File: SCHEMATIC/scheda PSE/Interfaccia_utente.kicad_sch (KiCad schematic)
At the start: 18 parts

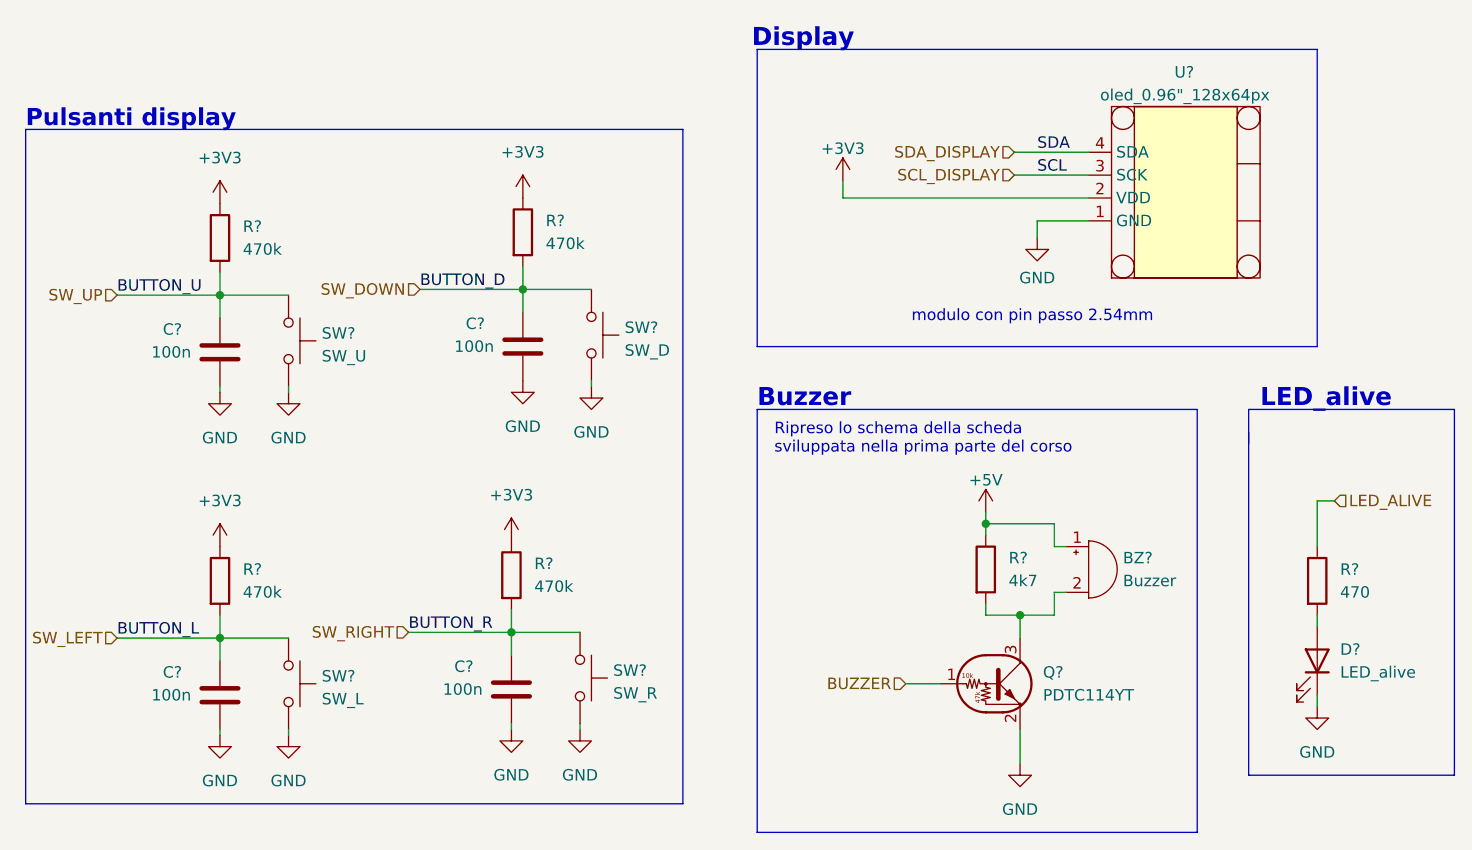
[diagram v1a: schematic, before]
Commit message: Aggiunti QUASI tutti i footprint
aggiunti quasi tutti i footprint dei componenti
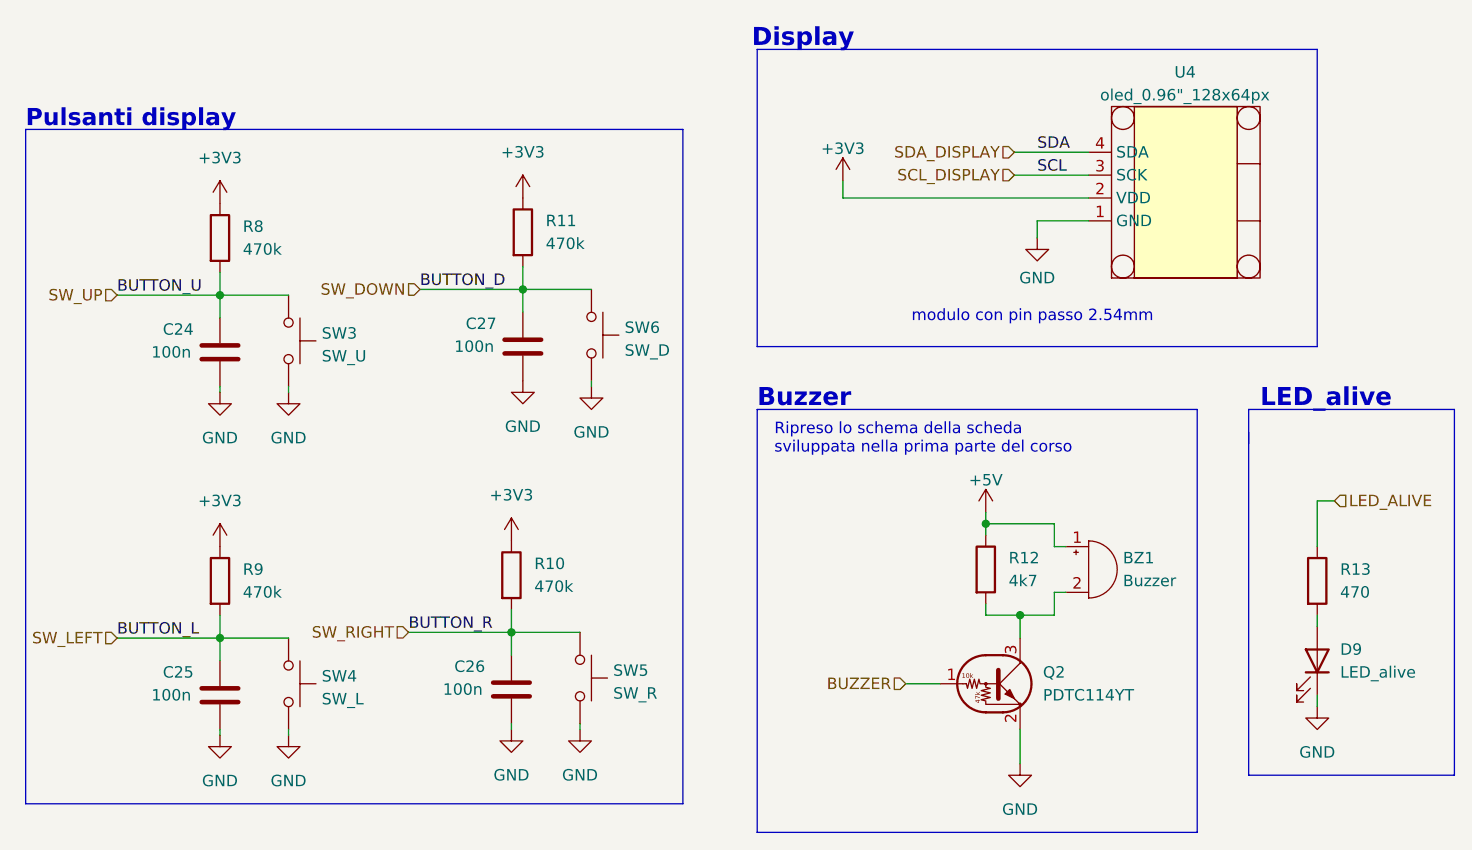
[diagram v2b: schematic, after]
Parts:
- C24, C25, C26, C27: renamed from C?; footprint (none) -> Capacitor_SMD:C_0603_1608Metric
- D9: renamed from D?; footprint (none) -> LED_SMD:LED_0603_1608Metric
- R10, R11, R13, R8, R9: renamed from R?; footprint (none) -> Resistor_SMD:R_0603_1608Metric
- SW3, SW4, SW5, SW6: renamed from SW?; footprint (none) -> Button_Switch_THT:SW_PUSH_6mm_H5mm
- U4: renamed from U?; footprint (none) -> _PSE:128x64OLED
- gave numbers to parts that had none: 3

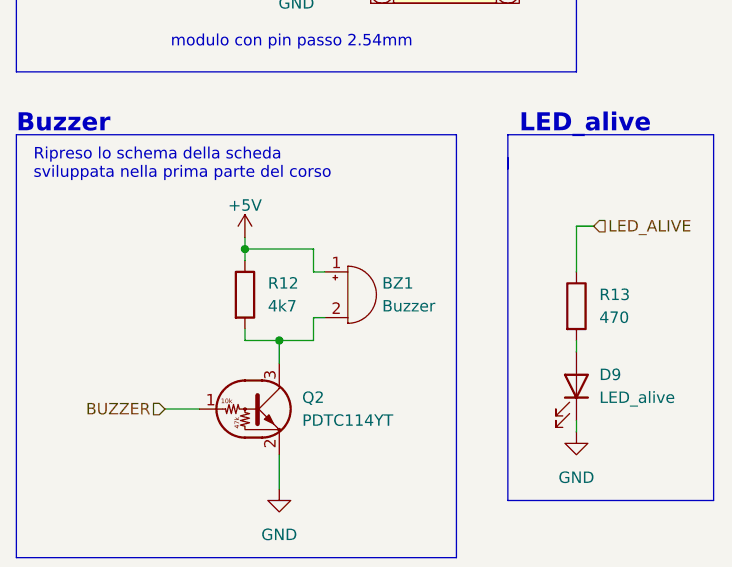
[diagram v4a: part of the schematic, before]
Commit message: sistemato buzzer, e continuato lo sbroglio
sistemato il buzzer con un altro footprint e ho continuato lo sbroglio.
Teoricamente manca solo collegare i collegamenti tra le gpio del rp2040 e il resto dei componenti
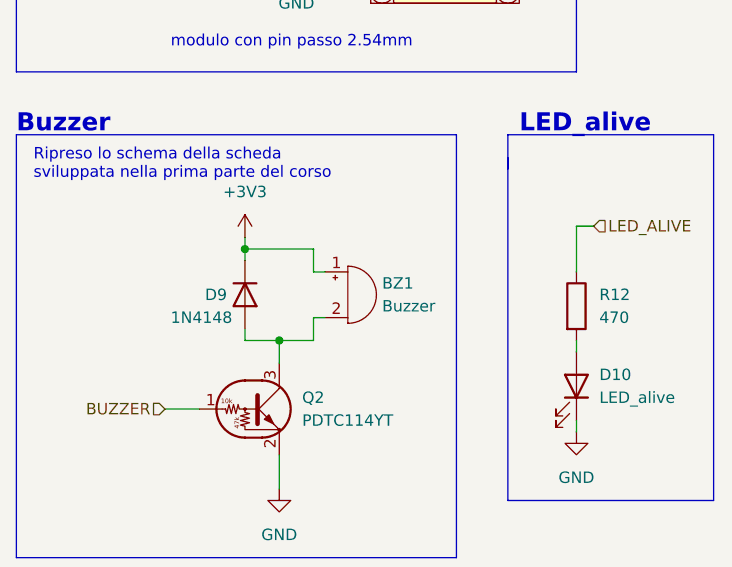
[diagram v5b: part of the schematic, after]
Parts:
- removed R12: 4k7, Resistor_SMD:R_0603_1608Metric, symbol Device:R
- added D9: 1N4148, Diode_SMD:D_SOD-123, symbol Diode:1N4148
- BZ1: footprint Buzzer_Beeper:MagneticBuzzer_Kingstate_KCG0601 -> _PSE:MLT-8530
- renumbered D9 to D10, R13 to R12
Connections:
- net +5V is gone; now on net +3V3: BZ1.1 (-)
- net +3V3: now also D9.1 (K)
- net at BZ1.2 (+), Q2.3 (C): now also D9.2 (A)
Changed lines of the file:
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@@
+    (pin "1")
+  )
+  (symbol (lib_id "power:+3V3") (at 187.96 98.425 0) (unit 1)
+    (in_bom yes) (on_board yes) (fields_autoplaced)
+    (property "Reference" "#PWR040" (id 0) (at 187.96 102.235 0)
+      (effects (font (size 1.27 1.27)) hide)
+    )
+    (property "Value" "+3V3" (id 1) (at 187.96 93.345 0))
+    (property "Footprint" "" (id 2) (at 187.96 98.425 0)
+      (effects (font (size 1.27 1.27)) hide)
+    )
+    (property "Datasheet" "" (id 3) (at 187.96 98.425 0)
+      (effects (font (size 1.27 1.27)) hide)
+    )
     (pin "1")
   )
@@
   (symbol (lib_id "Device:LED") (at 224.79 114.935 270) (mirror x) (unit 1)
     (in_bom yes) (on_board yes)
-    (property "Reference" "D9" (id 0) (at 227.33 113.665 90)
+    (property "Reference" "D10" (id 0) (at 227.33 113.665 90)
       (effects (font (size 1.27 1.27)) (justify left))
     )
@@
   (symbol (lib_id "Device:R") (at 224.79 106.045 0) (unit 1)
     (in_bom yes) (on_board yes) (fields_autoplaced)
-    (property "Reference" "R13" (id 0) (at 227.33 104.7749 0)
+    (property "Reference" "R12" (id 0) (at 227.33 104.7749 0)
       (effects (font (size 1.27 1.27)) (justify left))
     )
@@
     (pin "1")
   )
-  (symbol (lib_id "Device:R") (at 187.96 104.775 0) (unit 1)
-    (in_bom yes) (on_board yes) (fields_autoplaced)
-    (property "Reference" "R12" (id 0) (at 190.5 103.5049 0)
-      (effects (font (size 1.27 1.27)) (justify left))
-    )
-    (property "Value" "4k7" (id 1) (at 190.5 106.0449 0)
-      (effects (font (size 1.27 1.27)) (justify left))
-    )
-    (property "Footprint" "Resistor_SMD:R_0603_1608Metric" (id 2) (at 186.182 104.775 90)
-      (effects (font (size 1.27 1.27)) hide)
-    )
-    (property "Datasheet" "~" (id 3) (at 187.96 104.775 0)
+  (symbol (lib_id "Diode:1N4148") (at 187.96 104.775 270) (unit 1)
+    (in_bom yes) (on_board yes)
+    (property "Reference" "D9" (id 0) (at 183.515 104.775 90)
+      (effects (font (size 1.27 1.27)) (justify left))
+    )
+    (property "Value" "1N4148" (id 1) (at 179.705 107.315 90)
+      (effects (font (size 1.27 1.27)) (justify left))
+    )
+    (property "Footprint" "Diode_SMD:D_SOD-123" (id 2) (at 187.96 104.775 0)
+      (effects (font (size 1.27 1.27)) hide)
+    )
+    (property "Datasheet" "https://assets.nexperia.com/documents/data-sheet/1N4148_1N4448.pdf" (id 3) (at 187.96 104.775 0)
       (effects (font (size 1.27 1.27)) hide)
     )
@@
       (effects (font (size 1.27 1.27)) (justify left))
     )
-    (property "Footprint" "Buzzer_Beeper:MagneticBuzzer_Kingstate_KCG0601" (id 2) (at 198.755 102.235 90)
+    (property "Footprint" "_PSE:MLT-8530" (id 2) (at 198.755 102.235 90)
       (effects (font (size 1.27 1.27)) hide)
     )
@@
     (pin "2")
   )
-  (symbol (lib_id "power:+5V") (at 187.96 98.425 0) (unit 1)
-    (in_bom yes) (on_board yes) (fields_autoplaced)
-    (property "Reference" "#PWR040" (id 0) (at 187.96 102.235 0)
-      (effects (font (size 1.27 1.27)) hide)
-    )
-    (property "Value" "+5V" (id 1) (at 187.96 94.8492 0))
-    (property "Footprint" "" (id 2) (at 187.96 98.425 0)
-      (effects (font (size 1.27 1.27)) hide)
-    )
-    (property "Datasheet" "" (id 3) (at 187.96 98.425 0)
-      (effects (font (size 1.27 1.27)) hide)
-    )
-    (pin "1")
-  )
   (symbol (lib_id "Switch:SW_Push") (at 144.145 78.74 270) (unit 1)

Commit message: cambiati i pulsanti in smd
se servono gli altri pulsanti usare la versione precedente
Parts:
- SW3, SW4, SW5, SW6: footprint Button_Switch_THT:SW_PUSH_6mm_H5mm -> Button_Switch_SMD:SW_SPST_EVQP0
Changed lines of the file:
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@@
       (effects (font (size 1.27 1.27)) (justify left))
     )
-    (property "Footprint" "Button_Switch_THT:SW_PUSH_6mm_H5mm" (id 2) (at 149.225 78.74 0)
+    (property "Footprint" "Button_Switch_SMD:SW_SPST_EVQP0" (id 2) (at 149.225 78.74 0)
       (effects (font (size 1.27 1.27)) hide)
     )
@@
       (effects (font (size 1.27 1.27)) (justify left))
     )
-    (property "Footprint" "Button_Switch_THT:SW_PUSH_6mm_H5mm" (id 2) (at 147.955 116.84 0)
+    (property "Footprint" "Button_Switch_SMD:SW_SPST_EVQP0" (id 2) (at 147.955 116.84 0)
       (effects (font (size 1.27 1.27)) hide)
     )
@@
       (effects (font (size 1.27 1.27)) (justify left))
     )
-    (property "Footprint" "Button_Switch_THT:SW_PUSH_6mm_H5mm" (id 2) (at 115.57 79.375 0)
+    (property "Footprint" "Button_Switch_SMD:SW_SPST_EVQP0" (id 2) (at 115.57 79.375 0)
       (effects (font (size 1.27 1.27)) hide)
     )
@@
       (effects (font (size 1.27 1.27)) (justify left))
     )
-    (property "Footprint" "Button_Switch_THT:SW_PUSH_6mm_H5mm" (id 2) (at 115.57 117.475 0)
-      (effects (font (size 1.27 1.27)) hide)
-    )
+    (property "Footprint" "Button_Switch_SMD:SW_SPST_EVQP0" (id 2) (at 115.57 117.475 0)
+      (effects (font (size 1.27 1.27)) hide)
+    )

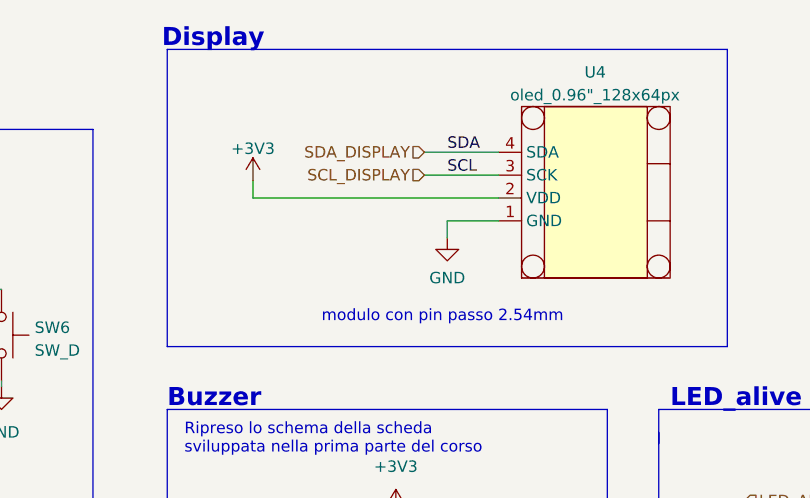
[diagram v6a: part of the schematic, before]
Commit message: Aggiunte tutte le cose richieste dal prof
Aggiunte tutte le cose richieste dal prof:
wifi
servo
uscita led
MANCA DA METERE IL SOLDER MASK SUI PAD NON USATI DEL GPS
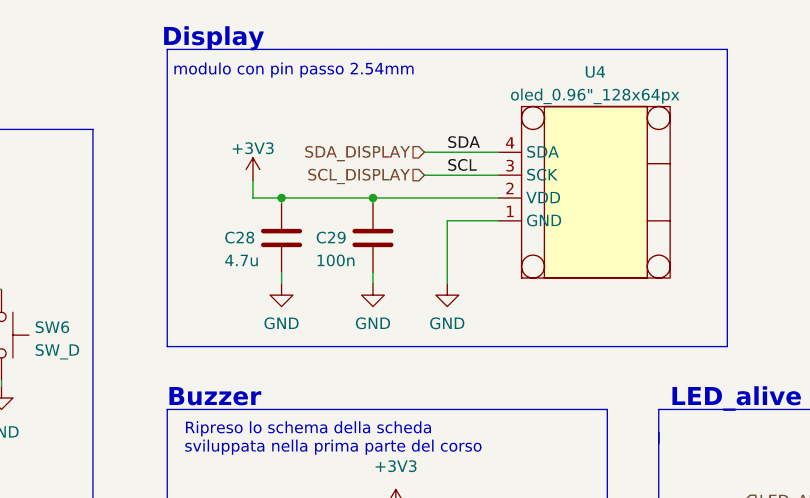
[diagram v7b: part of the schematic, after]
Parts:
- added C28: 4.7u, Capacitor_SMD:C_0603_1608Metric, symbol Device:C
- added C29: 100n, Capacitor_SMD:C_0603_1608Metric, symbol Device:C
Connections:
- net +3V3: now also C28.1, C29.1
- net GND: now also C28.2, C29.2
